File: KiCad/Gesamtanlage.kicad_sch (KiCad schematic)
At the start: 43 parts, among them J9 Conn_WallSocket_Earth, K1 power_contactor, K2 power_contactor, K3 power_contactor, T1 Siungle_Mikroinverter, T2 SR-ML2440, X1+ Reihenklemme_2-pol-verbunden, X2+ Reihenklemme_2-pol-verbunden, X3- Reihenklemme_3-pol-verbunden, X4 Reihenklemme_3-pol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

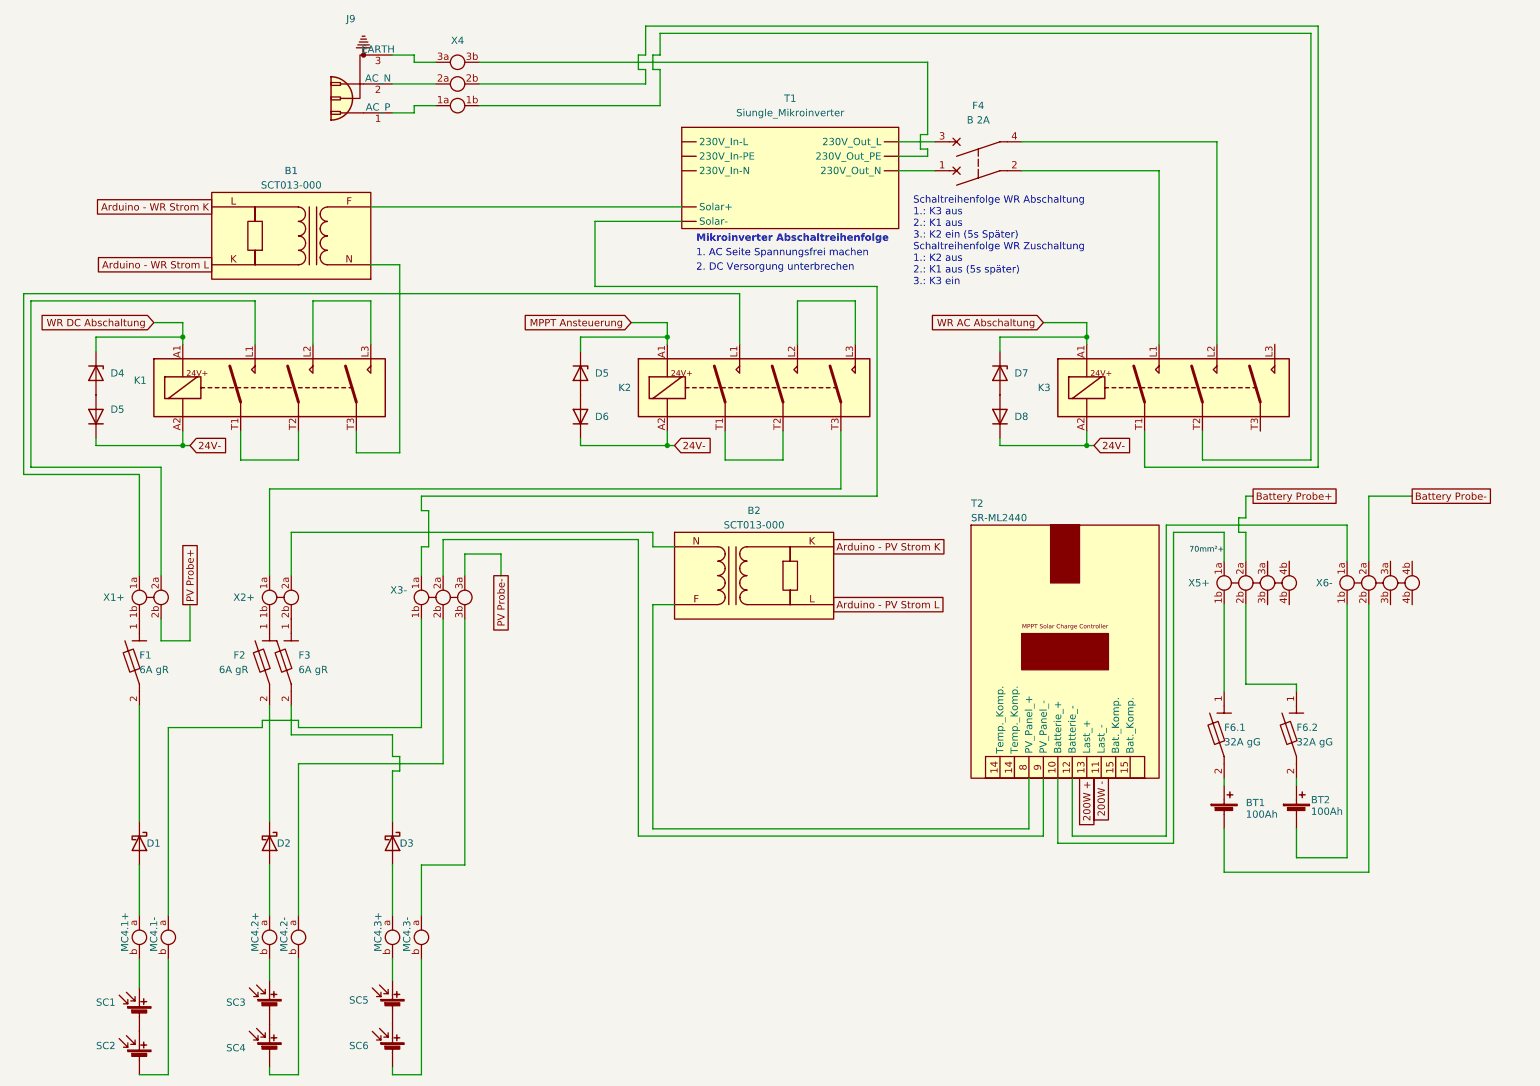
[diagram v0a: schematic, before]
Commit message: repository clean up | circuit diagram modified -> still have to add the wiring of the power supply in the circuit cabinet and the wiring of the UPS module
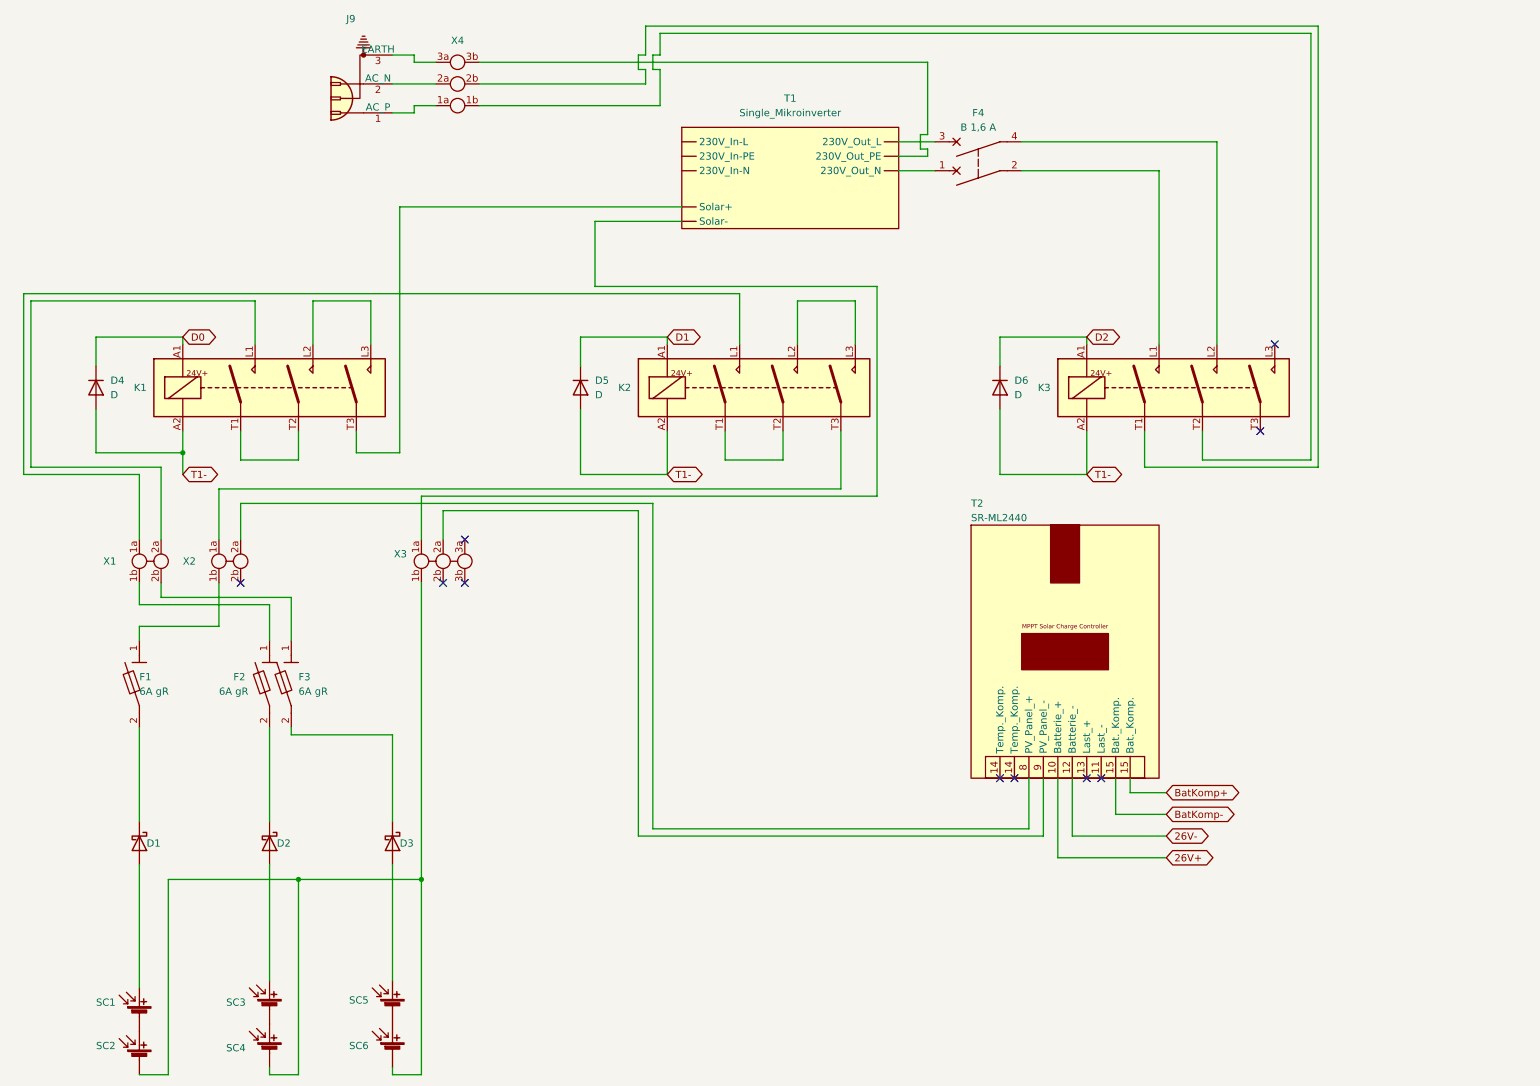
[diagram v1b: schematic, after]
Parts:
- removed B1, B2: SCT013-000, symbol AlexLib:SCT013-000
- removed BT1, BT2: 100Ah, symbol Device:Battery_Cell
- removed D4, D5, D7: D_Zener, symbol Device:D_Zener
- removed D5, D6, D8: ${SIM.PARAMS}, symbol Simulation_SPICE:DIODE
- removed F6.1, F6.2: 32A gG, symbol AlexLib:Sicherungstrennschalter 1 polig
- removed MC4.1+, MC4.1-, MC4.2+, MC4.2-, MC4.3+, MC4.3-: Reihenklemme, symbol AlexanderTonnLib:Reihenklemme
- removed X5+, X6-: Reihenklemme_4-pol, symbol AlexLib:Reihenklemme_4-pol
- added D4, D5, D6: D, symbol Device:D
- F4: value B 2A -> B 1,6 A
- T1: value Siungle_Mikroinverter -> Single_Mikroinverter
- renumbered X1+ to X1, X2+ to X2, X3- to X3
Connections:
- net PV Probe+ is gone; now on an unnamed net: X1.2b
- net at SC5.1 (+): now also D3.2 (A)
- net at X3.1b: now also SC2.2 (-), SC4.2 (-), SC6.2 (-)
- net at D1.2 (A): now also SC1.1 (+)
- net at T1. (Solar-): now also F4.3
- net at K1.T3: now also T1. (Solar-)
- net at F1.1: now also X2.1b; no longer X1.1b
- net 26V-: now reaches T2.12 (Batterie_-)
- net BatKomp-: now reaches T2.15 (Bat._Komp.)
- net at T2.8 (PV_Panel_+): now also X2.2a
- net at F2.1: now also X1.1b; no longer X2.1b
- net at F3.1: no longer X2.2b
- net at D2.2 (A): now also SC3.1 (+)
- net 200W +: no longer names the net of T2.13 (Last_+)
- net 200W -: no longer names the net of T2.11 (Last_-)
- net 24V- renamed T1-
- net T1-: now also D4.2 (A), D5.2 (A), D6.2 (A)
- net 70mm²+ renamed 26V+
- net MPPT Ansteuerung renamed D1
- net D1: now also D5.1 (K)
- net PV Probe-: no longer names the net of X3.3a
- net WR AC Abschaltung renamed D2
- net D2: now also D6.1 (K)
- net WR DC Abschaltung renamed D0
- net D0: now also D4.1 (K)
- new net BatKomp+: T2.15 (Bat._Komp.)
- no-connect marks 0 -> 10
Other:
- note removed: "1. AC Seite Spannungsfrei machen"
- note removed: "2. DC Versorgung unterbrechen"
- note removed: "Mikroinverter Abschaltreihenfolge"
- note removed: "Schaltreihenfolge WR Abschaltung 1.: K3 aus 2.: K1 aus 3.: K2 ein (5s Später) Schaltreihenfolge WR Zuschaltung 1.: K2 aus 2.: K1 aus (5s später) 3.: K3 ein"
- title: (none) -> Hauptstromlaufplan
- moved on the sheet: F1, F2, F3, X1, X2, X3
